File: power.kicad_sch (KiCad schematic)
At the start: 19 parts, among them IC3 CH224K, J5 USB_C_Receptacle_USB2.0, J6 Barrel_Jack, U20 TPS5430DDA, U9 AMS1117-3.3

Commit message: Add title to all schematics pages
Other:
- title: (none) -> Power
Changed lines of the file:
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@@
 	(paper "A4")
 	(title_block
+		(title "Power")
 		(rev "1")
 	)

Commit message: Redesign board to fit within 102mm x 102mm
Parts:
- C39, C57, J6, L14, R69: now left out of the parts list
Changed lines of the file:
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@@
 		(unit 1)
 		(exclude_from_sim no)
-		(in_bom yes)
+		(in_bom no)
 		(on_board yes)
 		(dnp no)
@@
 		(unit 1)
 		(exclude_from_sim no)
-		(in_bom yes)
+		(in_bom no)
 		(on_board yes)
 		(dnp no)
@@
 		(unit 1)
 		(exclude_from_sim no)
-		(in_bom yes)
+		(in_bom no)
 		(on_board yes)
 		(dnp no)
@@
 		(unit 1)
 		(exclude_from_sim no)
-		(in_bom yes)
+		(in_bom no)
 		(on_board yes)
 		(dnp no)
@@
 		(unit 1)
 		(exclude_from_sim no)
-		(in_bom yes)
-		(on_board yes)
-		(dnp no)
+		(in_bom no)
+		(on_board yes)
+		(dnp no)

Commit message: Update production data
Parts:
- IC3: now left out of the parts list
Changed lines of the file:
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@@
 		(unit 1)
 		(exclude_from_sim no)
-		(in_bom yes)
+		(in_bom no)
 		(on_board yes)
 		(dnp no)

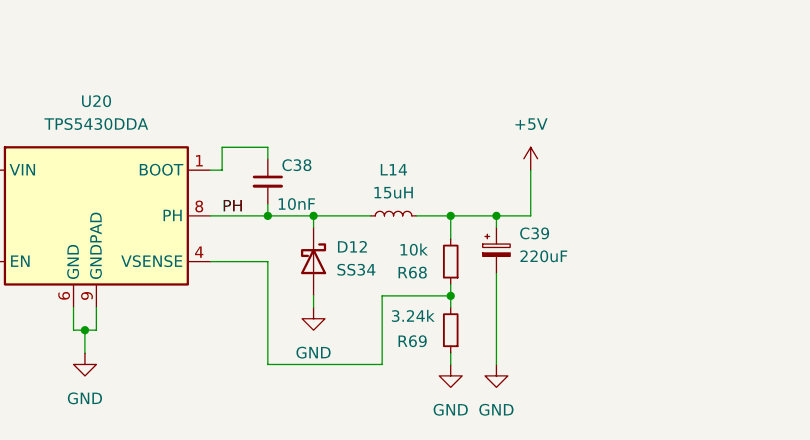
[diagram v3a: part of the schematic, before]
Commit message: Switch to basic components for 5V LDO feedback
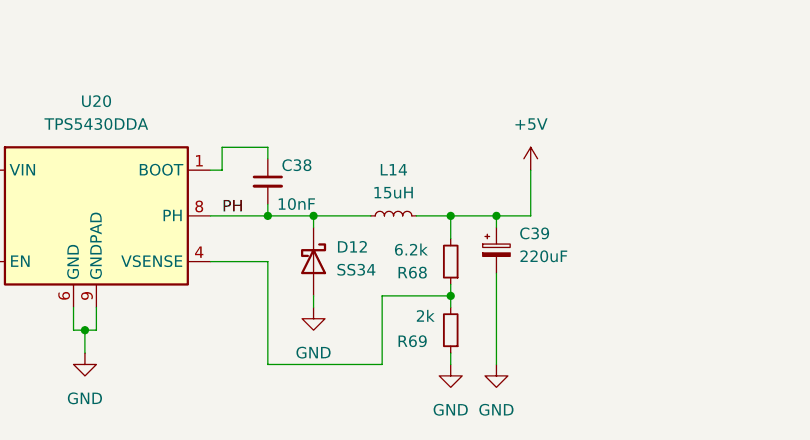
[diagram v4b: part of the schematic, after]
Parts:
- R68: value 10k -> 6.2k; LCSC C25804 -> C4260
- R69: value 3.24k -> 2k; LCSC C22994 -> C22975; now in the parts list
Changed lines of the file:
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@@
 			)
 		)
-		(property "Value" "10k"
+		(property "Value" "6.2k"
 			(at 90.17 172.7201 0)
 			(effects
@@
 			)
 		)
-		(property "LCSC" "C25804"
+		(property "LCSC" "C4260"
 			(at 92.71 173.99 0)
 			(effects
@@
 		(unit 1)
 		(exclude_from_sim no)
-		(in_bom no)
+		(in_bom yes)
 		(on_board yes)
 		(dnp no)
@@
 			)
 		)
-		(property "Value" "3.24k"
+		(property "Value" "2k"
 			(at 90.932 180.086 0)
 			(effects
@@
 			)
 		)
-		(property "LCSC" "C22994"
+		(property "LCSC" "C22975"
 			(at 92.71 181.61 0)
 			(effects

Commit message: Fix manufaturing properties
Such as rotations
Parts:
- C39, L14: now in the parts list
- IC3: JLCPCB Rotation Offset (none) -> 270; now in the parts list
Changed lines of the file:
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@@
 		(unit 1)
 		(exclude_from_sim no)
-		(in_bom no)
+		(in_bom yes)
 		(on_board yes)
 		(dnp no)
@@
 		(unit 1)
 		(exclude_from_sim no)
-		(in_bom no)
+		(in_bom yes)
 		(on_board yes)
 		(dnp no)
@@
 		(unit 1)
 		(exclude_from_sim no)
-		(in_bom no)
+		(in_bom yes)
 		(on_board yes)
 		(dnp no)
@@
 			(at 73.66 41.91 0)
 			(effects
+				(font
+					(size 1.27 1.27)
+				)
+				(hide yes)
+			)
+		)
+		(property "JLCPCB Rotation Offset" "270"
+			(at 73.66 41.91 0)
+			(effects

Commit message: Replace C57
With a variant that can be used with economy pcbs at JLCPCB
Closes #25
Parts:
- C57: footprint Capacitor_SMD:CP_Elec_4x5.4 -> Capacitor_SMD:CP_Elec_5x5.4; LCSC C72485 -> C30110; now in the parts list
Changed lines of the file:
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@@
 		(unit 1)
 		(exclude_from_sim no)
-		(in_bom no)
+		(in_bom yes)
 		(on_board yes)
 		(dnp no)
@@
 			)
 		)
-		(property "Footprint" "Capacitor_SMD:CP_Elec_4x5.4"
+		(property "Footprint" "Capacitor_SMD:CP_Elec_5x5.4"
 			(at 29.21 167.64 0)
 			(effects
@@
 			)
 		)
-		(property "LCSC" "C72485"
+		(property "LCSC" "C30110"
 			(at 29.21 167.64 0)
 			(effects
-				(font
-					(size 1.27 1.27)
-				)
-				(hide yes)
-			)
-		)
-		(property "LCSC alt" ""
-			(at 29.21 167.64 0)
-			(effects

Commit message: Replace DC connector with SMD variant
Closes #23
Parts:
- J6: footprint Connector_BarrelJack:BarrelJack_Horizontal -> Connector_BarrelJack:BarrelJack_CLIFF_FC681465S_SMT_Horizontal; LCSC C381115 -> C431534; now in the parts list
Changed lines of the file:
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@@
 		(unit 1)
 		(exclude_from_sim no)
-		(in_bom no)
+		(in_bom yes)
 		(on_board yes)
 		(dnp no)
@@
 			)
 		)
-		(property "Footprint" "Connector_BarrelJack:BarrelJack_Horizontal"
+		(property "Footprint" "Connector_BarrelJack:BarrelJack_CLIFF_FC681465S_SMT_Horizontal"
 			(at 144.78 36.576 0)
 			(effects
@@
 			)
 		)
-		(property "LCSC" "C381115"
+		(property "LCSC" "C431534"
 			(at 143.51 35.56 0)
 			(effects
-				(font
-					(size 1.27 1.27)
-				)
-				(hide yes)
-			)
-		)
-		(property "LCSC alt" ""
-			(at 143.51 35.56 0)
-			(effects

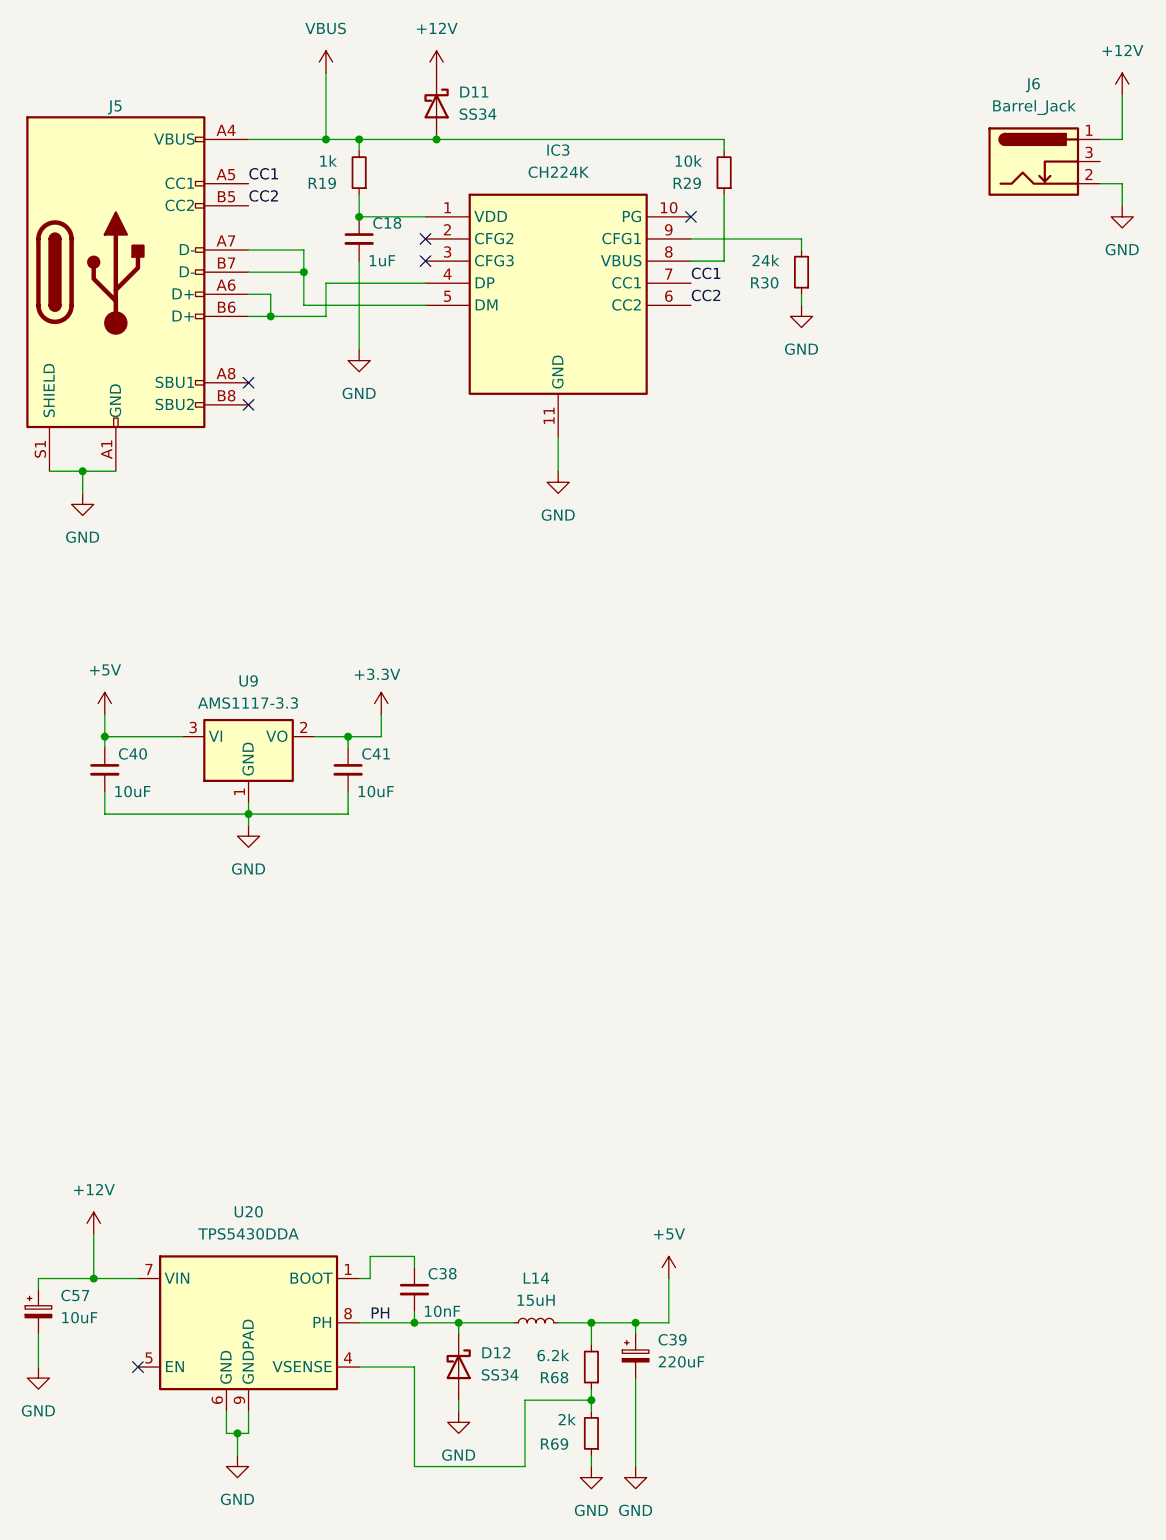
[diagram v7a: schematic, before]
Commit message: Route USB data signals to STM32
The CANbus needed to be moved together with ec and ph disable signals.
Closes #14 and #9
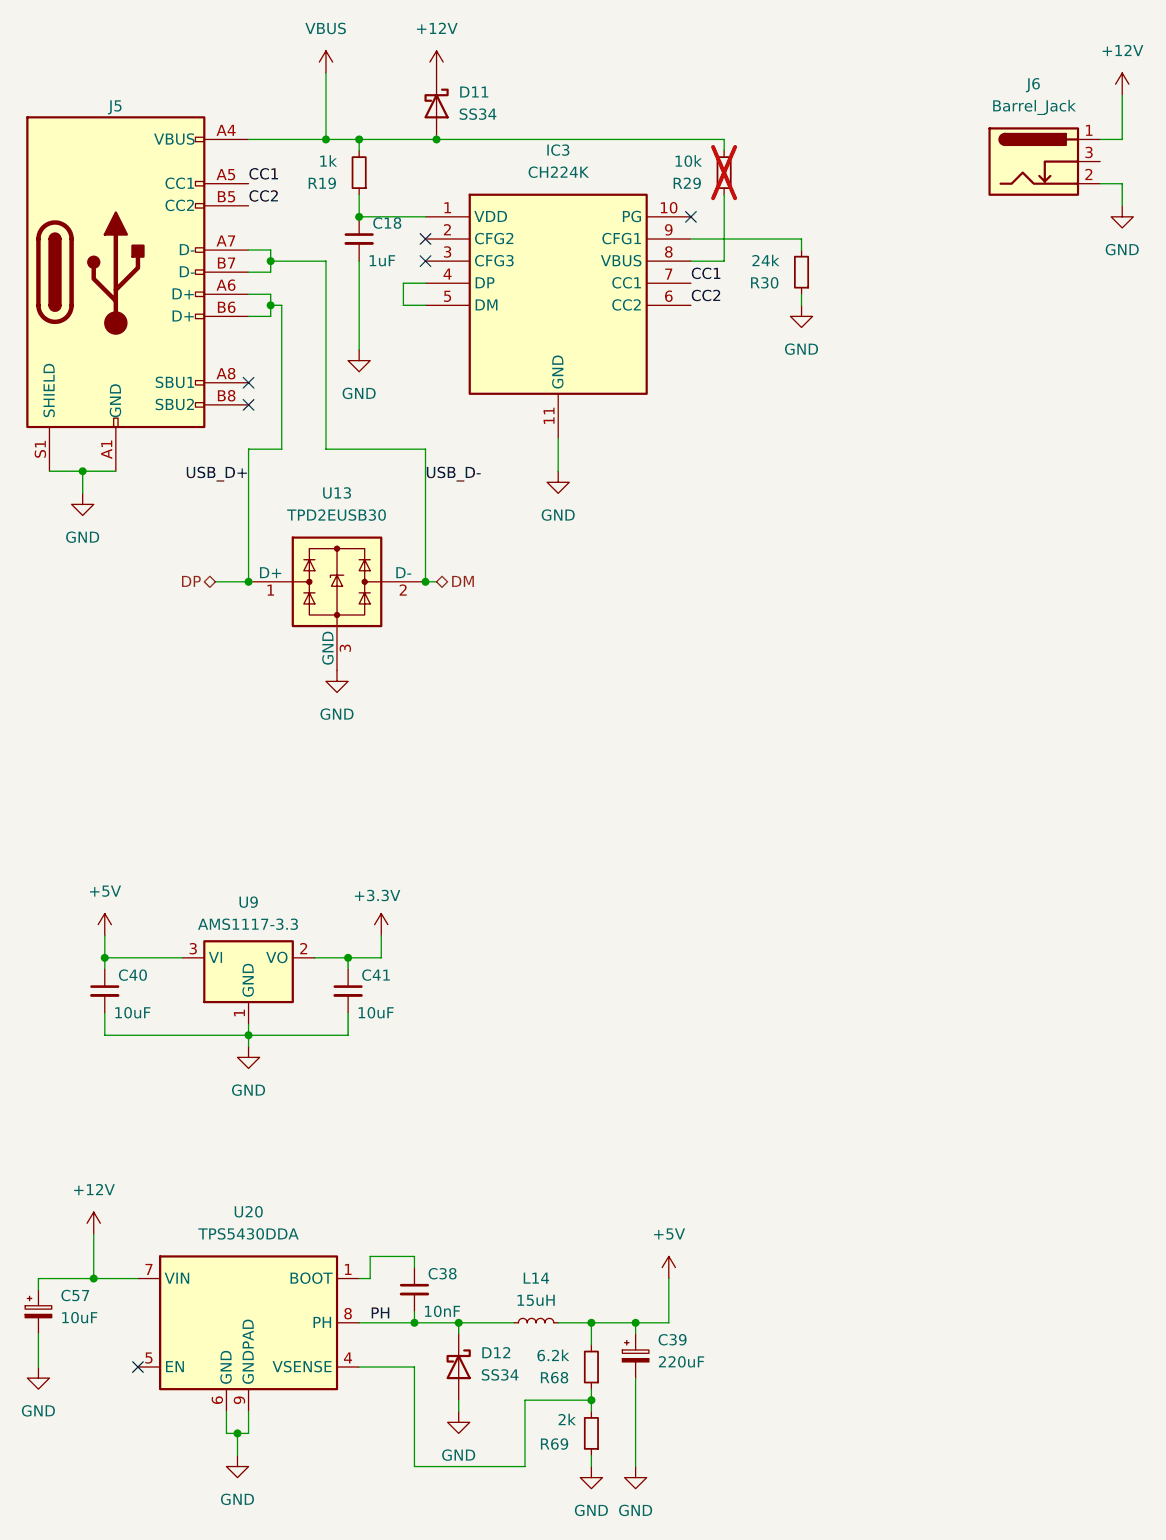
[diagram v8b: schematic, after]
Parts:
- added U13: TPD2EUSB30, Package_TO_SOT_SMD:Texas_DRT-3, symbol Power_Protection:TPD2EUSB30
- R29: now not fitted; now left out of the parts list
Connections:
- net GND: now also U13.3 (GND)
- net DP: now reaches J5.A6 (D+), J5.B6 (D+)
- net DP: now also U13.1 (D+); no longer IC3.4 (DP)
- net DM: now reaches J5.A7 (D-), J5.B7 (D-)
- net DM: now also U13.2 (D-); no longer IC3.5 (DM)
- new net: IC3.4 (DP), IC3.5 (DM)
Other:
- moved on the sheet: C40, C41, U9
